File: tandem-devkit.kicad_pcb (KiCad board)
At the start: 2 copper layers, 95.4 x 100 mm, 88 parts, among them J101 Conn_01x02, J102 QWIIC I2C Connector, J301 ConnectorLCDFrontLight, J302 FPC24(0.5MM), J303 FPC10(0.5MM), Q301 2N7002, Q302 2N7002, Q303 AO3401A, U201 AMS1117-ADJ_SOT223

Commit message: PCB: update netlist
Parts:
- renumbered R113 to R107, R107 to R108, R108 to R109, R112 to R110, R109 to R112, R110 to R113
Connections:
- A101 pad 10: Net-(A101-Pad10) -> /LCD_CURRENT_SENSE
- A101 pad 19: /CAP_TOUCH_2 -> Net-(A101-Pad19)
- A101 pad 20: Net-(A101-Pad20) -> unconnected-(A101-Pad20)
- A101 pad 25: /CAP_TOUCH_3 -> Net-(A101-Pad25)
- A101 pad 6: /EPD_CURRENT_SENSE -> /CAP_TOUCH_2
- A101 pad 7: /LCD_CURRENT_SENSE -> /CAP_TOUCH_3
- A101 pad 8: Net-(A101-Pad8) -> /CAP_TOUCH_4
- A101 pad 9: Net-(A101-Pad9) -> /EPD_CURRENT_SENSE
- A102 pad 10: Net-(A101-Pad10) -> /LCD_CURRENT_SENSE
- A102 pad 19: /CAP_TOUCH_2 -> Net-(A101-Pad19)
- A102 pad 20: Net-(A101-Pad20) -> unconnected-(A101-Pad20)
- A102 pad 25: /CAP_TOUCH_3 -> Net-(A101-Pad25)
- A102 pad 6: /EPD_CURRENT_SENSE -> /CAP_TOUCH_2
- A102 pad 7: /LCD_CURRENT_SENSE -> /CAP_TOUCH_3
- A102 pad 8: Net-(A101-Pad8) -> /CAP_TOUCH_4
- A102 pad 9: Net-(A101-Pad9) -> /EPD_CURRENT_SENSE
- R102 pad 2: Net-(A101-Pad20) -> Net-(A101-Pad19)
- R107 pad 2: Net-(A101-Pad10) -> Net-(A101-Pad25)
- R110 pad 2: Net-(A101-Pad9) -> Net-(A101-Pad15)
- R111 pad 2: Net-(A101-Pad8) -> Net-(A101-Pad16)
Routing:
- net Net-(A101-Pad9): track 6.13 -> 0.00 mm
- net Net-(A101-Pad10): track 6.13 -> 0.00 mm
- net Net-(A101-Pad25): track 0.00 -> 6.13 mm
- net Net-(A101-Pad19): track 0.00 -> 6.13 mm
- net Net-(A101-Pad8): track 6.13 -> 0.00 mm
- net /CAP_TOUCH_4: track 0.00 -> 6.13 mm

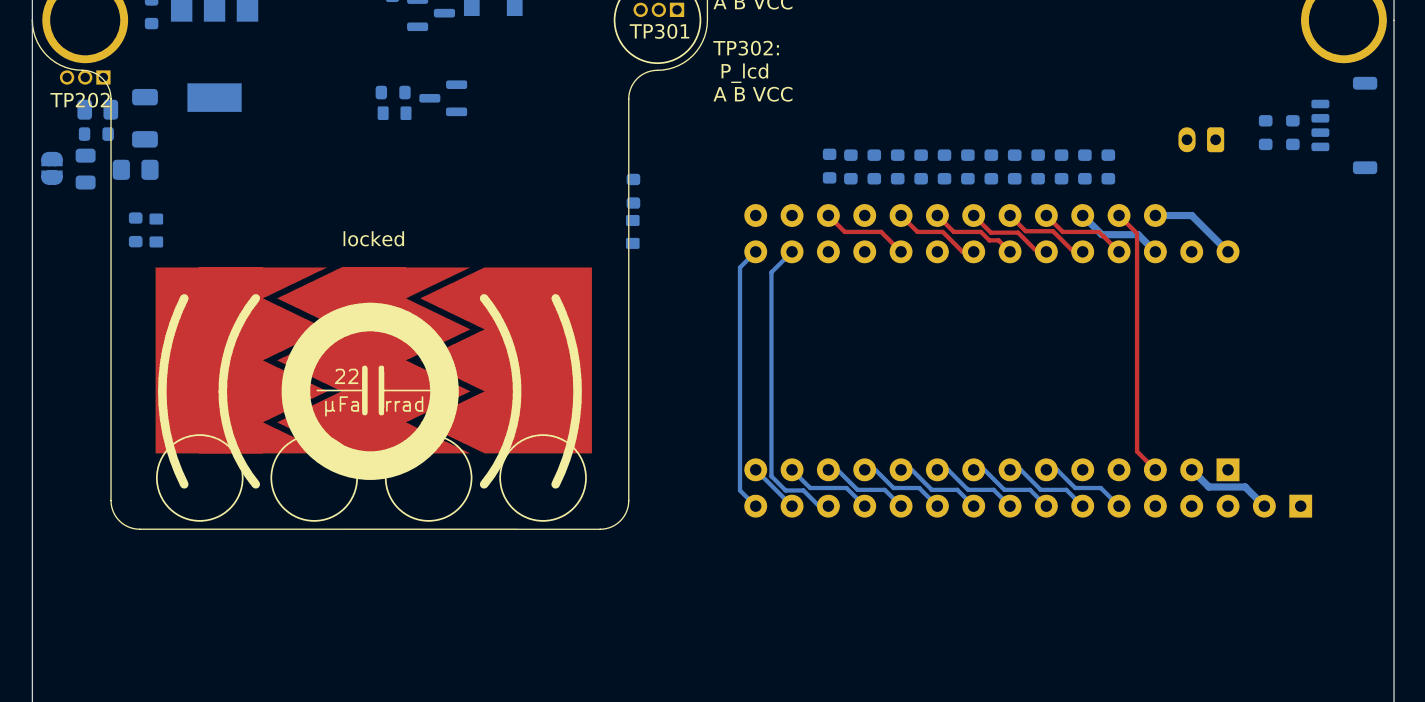
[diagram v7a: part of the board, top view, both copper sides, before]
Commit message: PCB: reorder a little, move all feather/itsy-bitsy internal connections to single copper layer
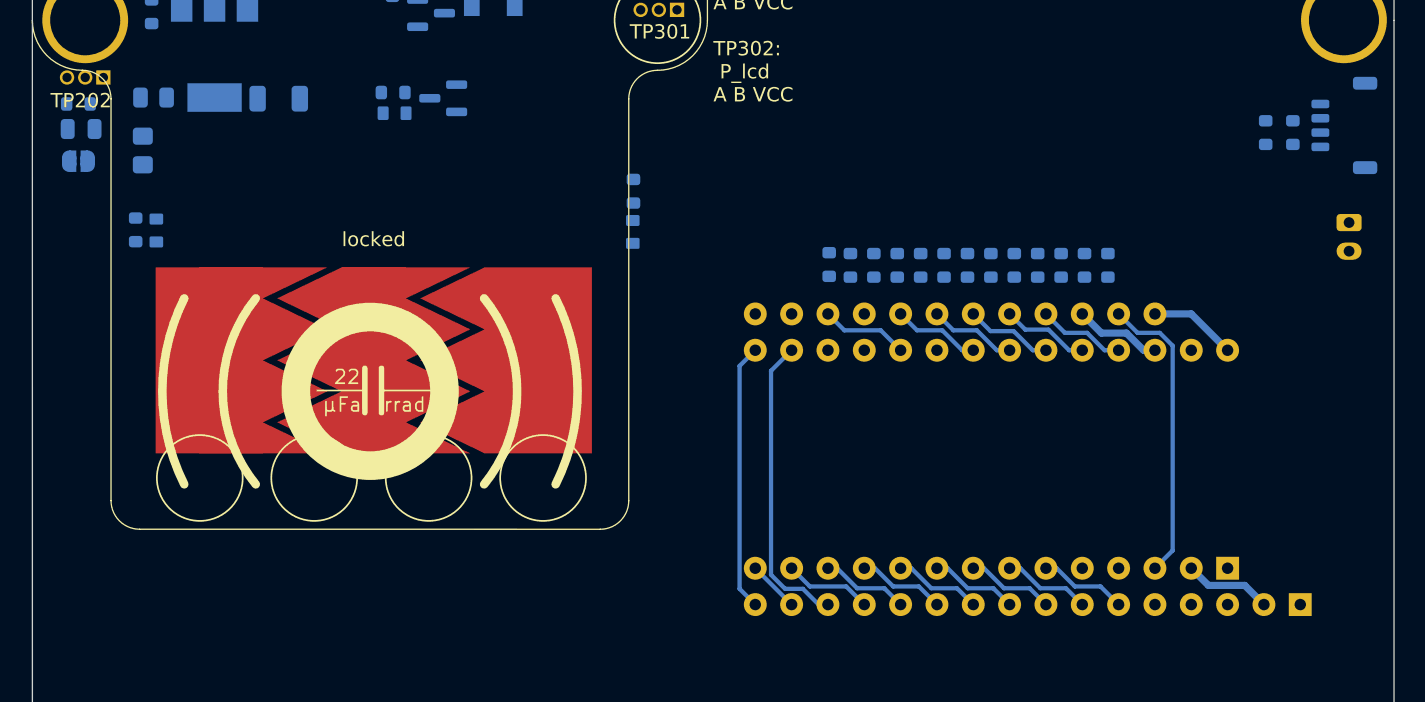
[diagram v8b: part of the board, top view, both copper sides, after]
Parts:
- moved J101 11.0 mm to (211.8, 73.3), turned to -90 degrees
- moved C205 9.45 mm to (137.0, 64.6), turned to 0 degrees
- moved A101 6.88 mm to (203.3, 97.5)
- moved A102 6.88 mm to (208.4, 100.0)
- moved R101 6.88 mm to (175.5, 76.2)
- moved R102 6.88 mm to (183.5, 76.3)
- moved R103 6.88 mm to (186.8, 76.3)
- moved R104 6.88 mm to (190.1, 76.3)
- moved R105 6.88 mm to (193.3, 76.3)
- moved R106 6.88 mm to (195.0, 76.3)
- moved R107 6.88 mm to (185.2, 76.3)
- moved R108 6.88 mm to (181.9, 76.3)
- moved R109 6.88 mm to (180.2, 76.3)
- moved R110 6.88 mm to (188.4, 76.3)
- moved R111 6.88 mm to (191.7, 76.3)
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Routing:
- net /SOM_PWR_EN: track 18.8 -> 20.8 mm
